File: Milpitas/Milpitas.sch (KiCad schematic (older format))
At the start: 0 parts

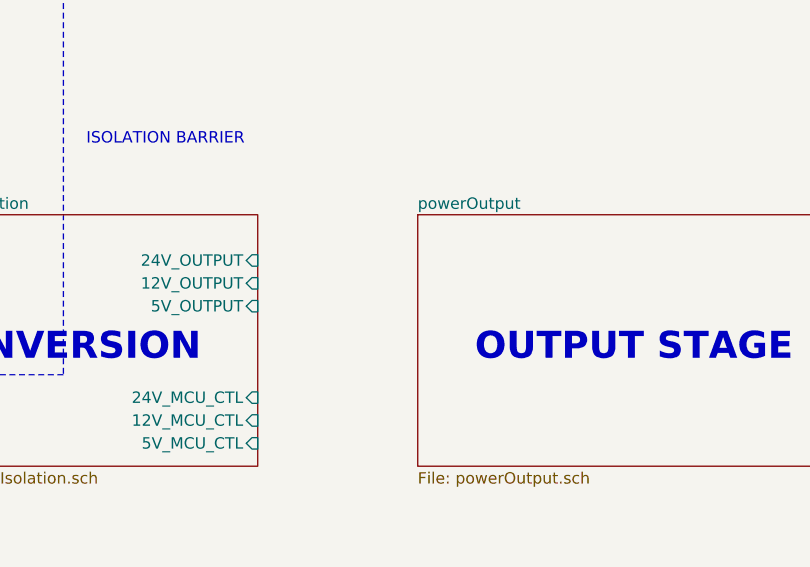
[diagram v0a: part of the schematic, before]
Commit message: Updated some silly mistakes
Updated some silly mistakes,
- capacitor decoupled to gnd
- Added option for jumper control to 2 24V modules
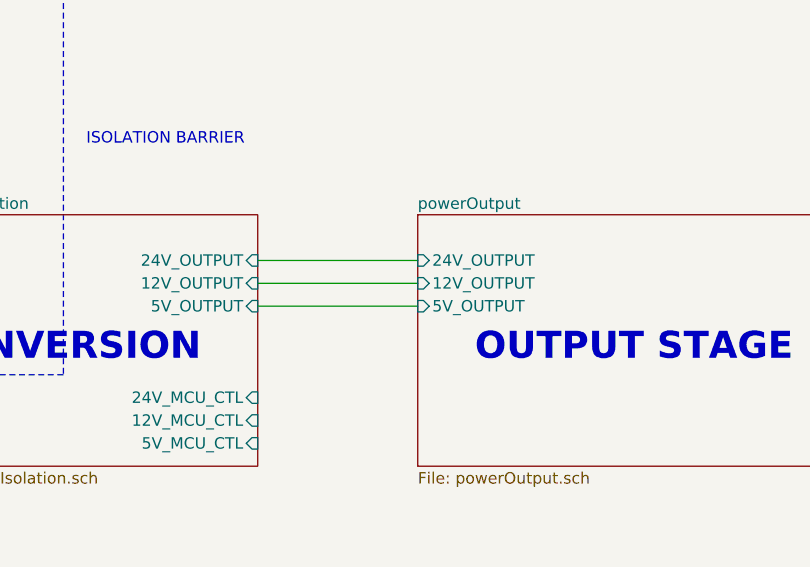
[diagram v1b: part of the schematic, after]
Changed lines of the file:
@@
 EESchema Schematic File Version 4
 LIBS:Milpitas-cache
-EELAYER 26 0
+EELAYER 29 0
 EELAYER END
 $Descr A4 11693 8268
@@
 F0 "powerOutput" 50
 F1 "powerOutput.sch" 50
+F2 "24V_OUTPUT" I L 7550 2550 50
+F3 "12V_OUTPUT" I L 7550 2650 50
+F4 "5V_OUTPUT" I L 7550 2750 50
 $EndSheet
 Text Notes 7800 3000 0    118  ~ 24
@@
 ISOLATION BARRIER
 $Comp
-L power:+5VP #PWR?
+L Milpitas-rescue:+5VP-power #PWR?
 U 1 1 5DD759BA
 P 3150 1650
@@
 $EndComp
 $Comp
-L power:GNDS #PWR?
+L Milpitas-rescue:GNDS-power #PWR?
 U 1 1 5DD75A22
 P 3500 1500
@@
 Wire Notes Line
 	3600 3950 500  3950
+Wire Wire Line
+	6850 2550 7550 2550
+Wire Wire Line
+	6850 2650 7550 2650
+Wire Wire Line
+	6850 2750 7550 2750
 $EndSCHEMATC

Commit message: Updated input control circuitry. Rationale and calcs in google drive.
Updated and added all part numbers for input protection circuitry. Not yet ready for review.
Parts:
- added MH? (x4): MountingHole, symbol Mechanical:MountingHole_Pad
- added R? (x4): R, symbol Device:R
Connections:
- net labels added: GND
- net labels removed: +5VP, GNDS
- wire segments 5 -> 40
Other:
- note removed: "INPUT SIDE POWER FLAGS\n"
- note removed: "ISOLATION BARRIER"
